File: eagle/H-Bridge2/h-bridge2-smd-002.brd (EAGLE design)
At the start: 100 x 80 mm, 36 parts

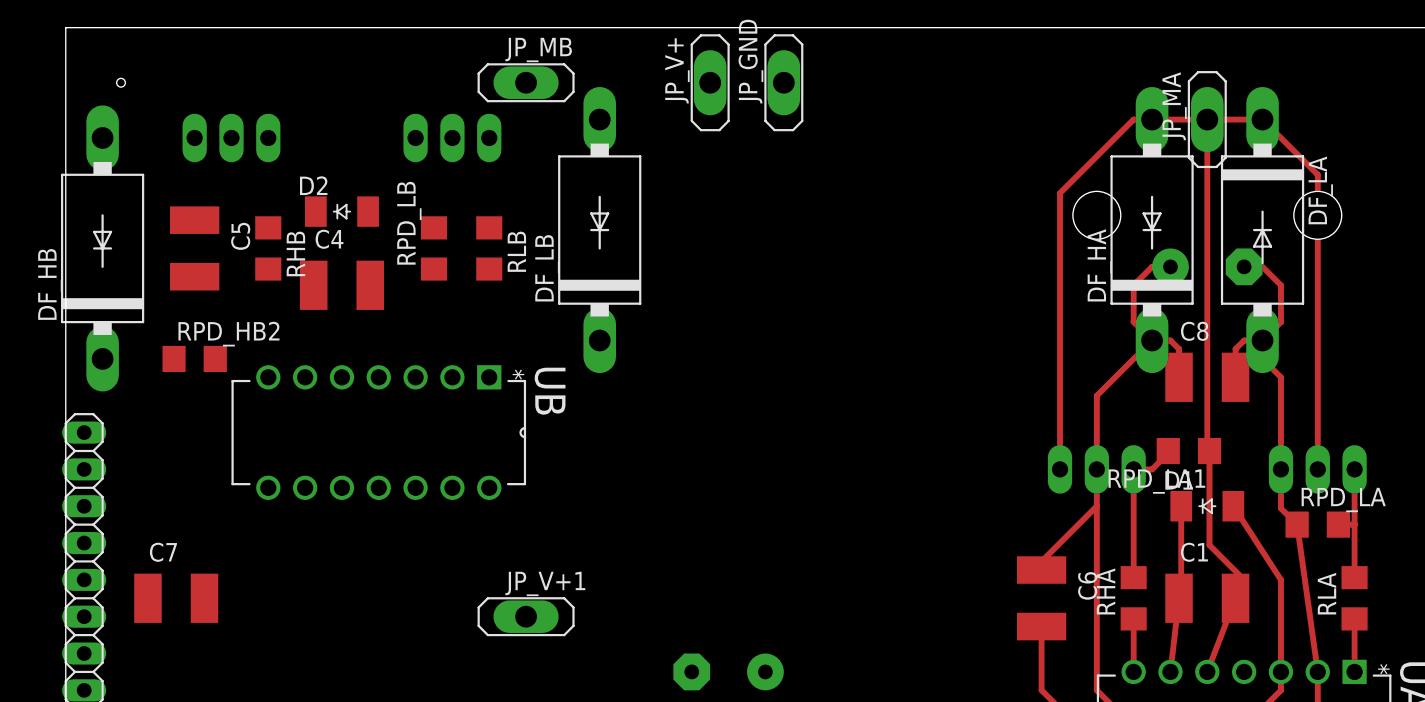
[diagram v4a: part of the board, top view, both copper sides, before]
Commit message: SMD for logic drv
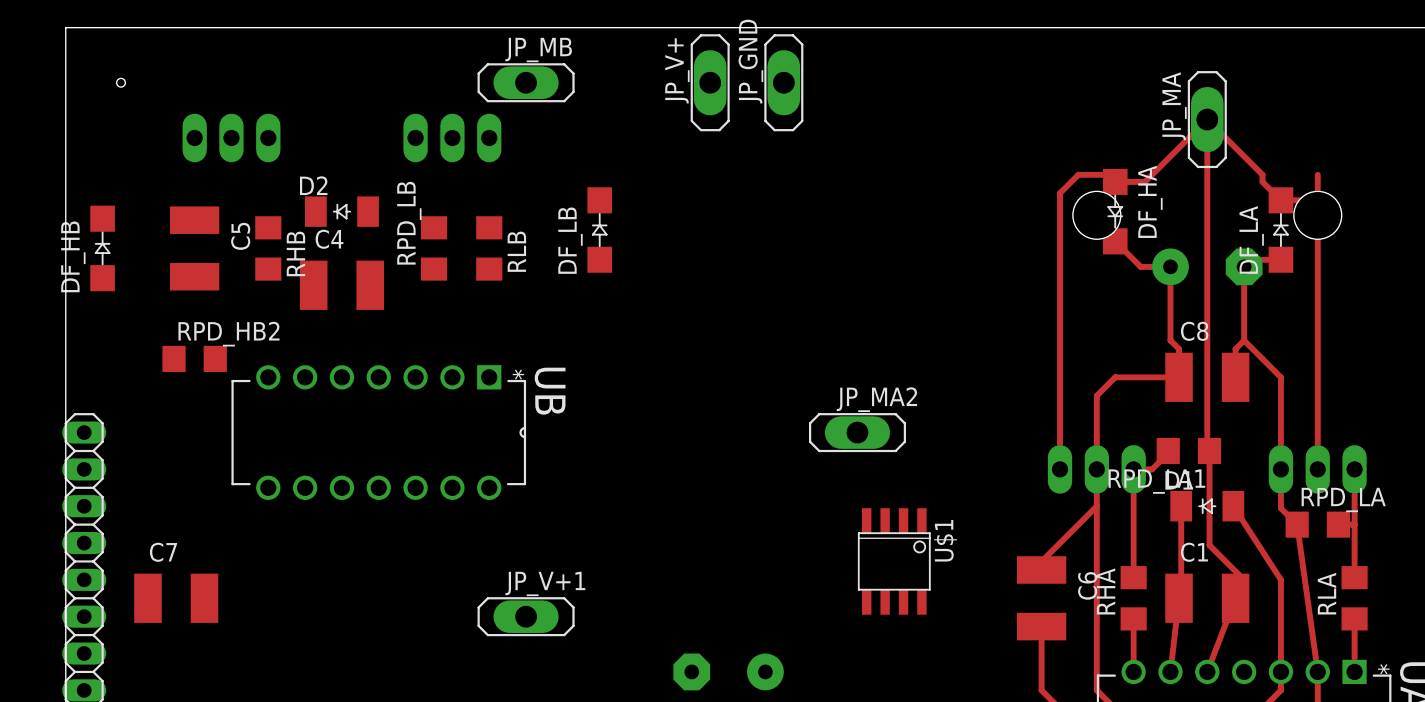
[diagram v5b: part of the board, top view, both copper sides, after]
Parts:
- added JP_MA2: (no value), dbg-misc:1X01
- added U$1: ACS711, acs711:SOIC8
- DF_HA, DF_HB, DF_LA, DF_LB: value 1N5400 -> GF1; device dbg-misc:DO201-15 -> diode:SMA-DO214AC
- moved DF_HA 2.84 mm to (72.4, 67.3), turned to 270 degrees
- moved DF_LA 1.27 mm to (83.8, 66.0), turned to 90 degrees
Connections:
- new net N$1: JP_MA2.1, U$1.3, U$1.4
- net N$13: now also DF_HA.K, DF_HB.K; no longer DF_HA.C, DF_HB.C
- net N$16: now also DF_LB.K; no longer DF_LB.C
- net N$17: now also DF_LA.K, U$1.1, U$1.2; no longer DF_LA.C
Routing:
- net N$13: track 71.1 -> 74.1 mm
- net N$17: track 100.6 -> 102.2 mm
- net N$4: track 67.5 -> 68.4 mm
